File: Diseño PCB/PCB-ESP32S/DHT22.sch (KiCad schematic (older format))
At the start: 2 parts

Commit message: esp-32 actualizacion
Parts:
- R3: footprint Resistor_SMD:R_0201_0603Metric -> Resistor_SMD:R_0805_2012Metric_Pad1.20x1.40mm_HandSolder
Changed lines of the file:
@@
 F 0 "R3" H 2420 2696 50  0000 L CNN
 F 1 "1k" H 2420 2605 50  0000 L CNN
-F 2 "Resistor_SMD:R_0201_0603Metric" V 2280 2650 50  0001 C CNN
+F 2 "Resistor_SMD:R_0805_2012Metric_Pad1.20x1.40mm_HandSolder" V 2280 2650 50  0001 C CNN
 F 3 "~" H 2350 2650 50  0001 C CNN
 	1    2350 2650

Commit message: .
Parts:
- TH1: symbol PCB-ESP32S-rescue:DHT22_Temperature_Humidity-sensors -> PCB-ESP32S-rescue:DHT22_Temperature_Humidity-sensors-PCB-ESP32S-rescue
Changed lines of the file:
@@
 $EndDescr
 $Comp
-L PCB-ESP32S-rescue:DHT22_Temperature_Humidity-sensors TH?
+L PCB-ESP32S-rescue:DHT22_Temperature_Humidity-sensors-PCB-ESP32S-rescue TH?
 U 1 1 61A00323
 P 2500 2350

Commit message: Actualización footprints
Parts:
- TH1: symbol PCB-ESP32S-rescue:DHT22_Temperature_Humidity-sensors-PCB-ESP32S-rescue -> PCB-ESP32S-rescue:DHT22_Temperature_Humidity-sensors-PCB-ESP32S-rescue-PCB-ESP32S-rescue
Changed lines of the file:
@@
 $EndDescr
 $Comp
-L PCB-ESP32S-rescue:DHT22_Temperature_Humidity-sensors-PCB-ESP32S-rescue TH?
+L PCB-ESP32S-rescue:DHT22_Temperature_Humidity-sensors-PCB-ESP32S-rescue-PCB-ESP32S-rescue TH?
 U 1 1 61A00323
 P 2500 2350

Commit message: pcv v2
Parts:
- TH1: footprint Sensors:DHT22_Temperature_Humidity -> Connector_JST:JST_GH_BM04B-GHS-TBT_1x04-1MP_P1.25mm_Vertical
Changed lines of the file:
@@
 F 0 "TH1" H 2778 2820 60  0000 L CNN
 F 1 "DHT22_Temperature_Humidity" H 2778 2714 60  0000 L CNN
-F 2 "Sensors:DHT22_Temperature_Humidity" H 2500 2350 60  0000 C CNN
+F 2 "Connector_JST:JST_GH_BM04B-GHS-TBT_1x04-1MP_P1.25mm_Vertical" H 2500 2350 60  0000 C CNN
 F 3 "" H 2500 2350 60  0000 C CNN
 	1    2500 2350

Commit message: mejoras pcb1
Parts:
- renumbered R3 to R8
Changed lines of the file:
@@
 P 2350 2650
 AR Path="/61A00339" Ref="R?"  Part="1"
-AR Path="/61A137FE/61A00339" Ref="R3"  Part="1"
-F 0 "R3" H 2420 2696 50  0000 L CNN
+AR Path="/61A137FE/61A00339" Ref="R8"  Part="1"
+F 0 "R8" H 2420 2696 50  0000 L CNN
 F 1 "1k" H 2420 2605 50  0000 L CNN
 F 2 "Resistor_SMD:R_0805_2012Metric_Pad1.20x1.40mm_HandSolder" V 2280 2650 50  0001 C CNN

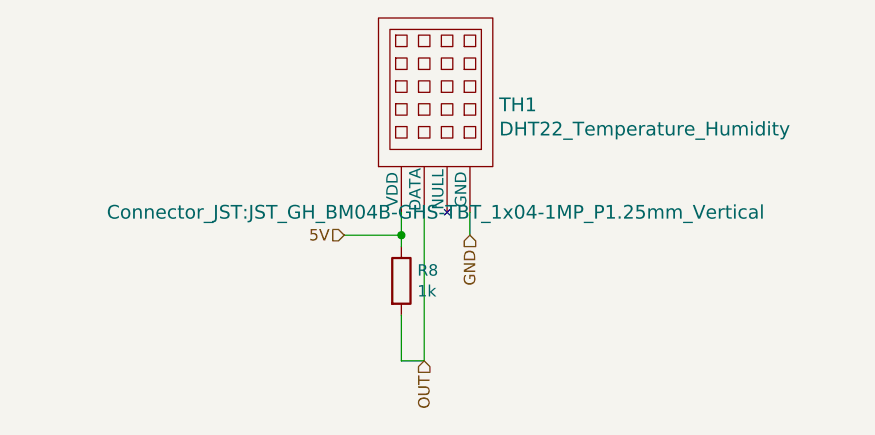
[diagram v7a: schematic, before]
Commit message: edicion true hole
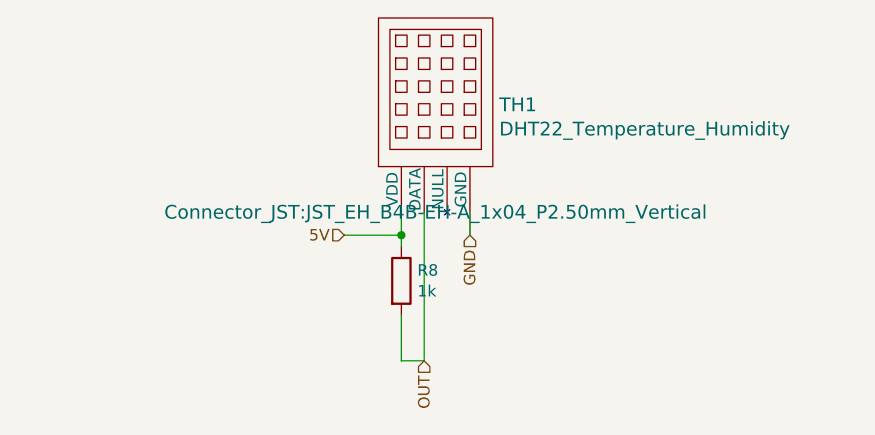
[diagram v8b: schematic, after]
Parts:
- TH1: footprint Connector_JST:JST_GH_BM04B-GHS-TBT_1x04-1MP_P1.25mm_Vertical -> Connector_JST:JST_EH_B4B-EH-A_1x04_P2.50mm_Vertical
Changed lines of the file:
@@
 F 0 "TH1" H 2778 2820 60  0000 L CNN
 F 1 "DHT22_Temperature_Humidity" H 2778 2714 60  0000 L CNN
-F 2 "Connector_JST:JST_GH_BM04B-GHS-TBT_1x04-1MP_P1.25mm_Vertical" H 2500 2350 60  0000 C CNN
+F 2 "Connector_JST:JST_EH_B4B-EH-A_1x04_P2.50mm_Vertical" H 2500 2350 60  0000 C CNN
 F 3 "" H 2500 2350 60  0000 C CNN
 	1    2500 2350
